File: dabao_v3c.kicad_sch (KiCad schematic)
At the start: 67 parts, among them J1 USB_C_Receptacle_USB2.0_16P, Q1 LP0404N3T5G, Q2 LN237N3T5G, SW1 SKTAAAE010, SW2 SKTAAAE010, U1 baochip1x, U3 SMD IC PMIC;DCDC Buck-ADJ-1A,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, U4 XIAO-HALF-HOLE-23P, U5 EMS4000RSW, U7 SGM40567-4.2XG/TR, U8 SX1801CCR, U9 SMD IC PMIC;DCDC Buck-ADJ-1A,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, Y2 48.000MHz

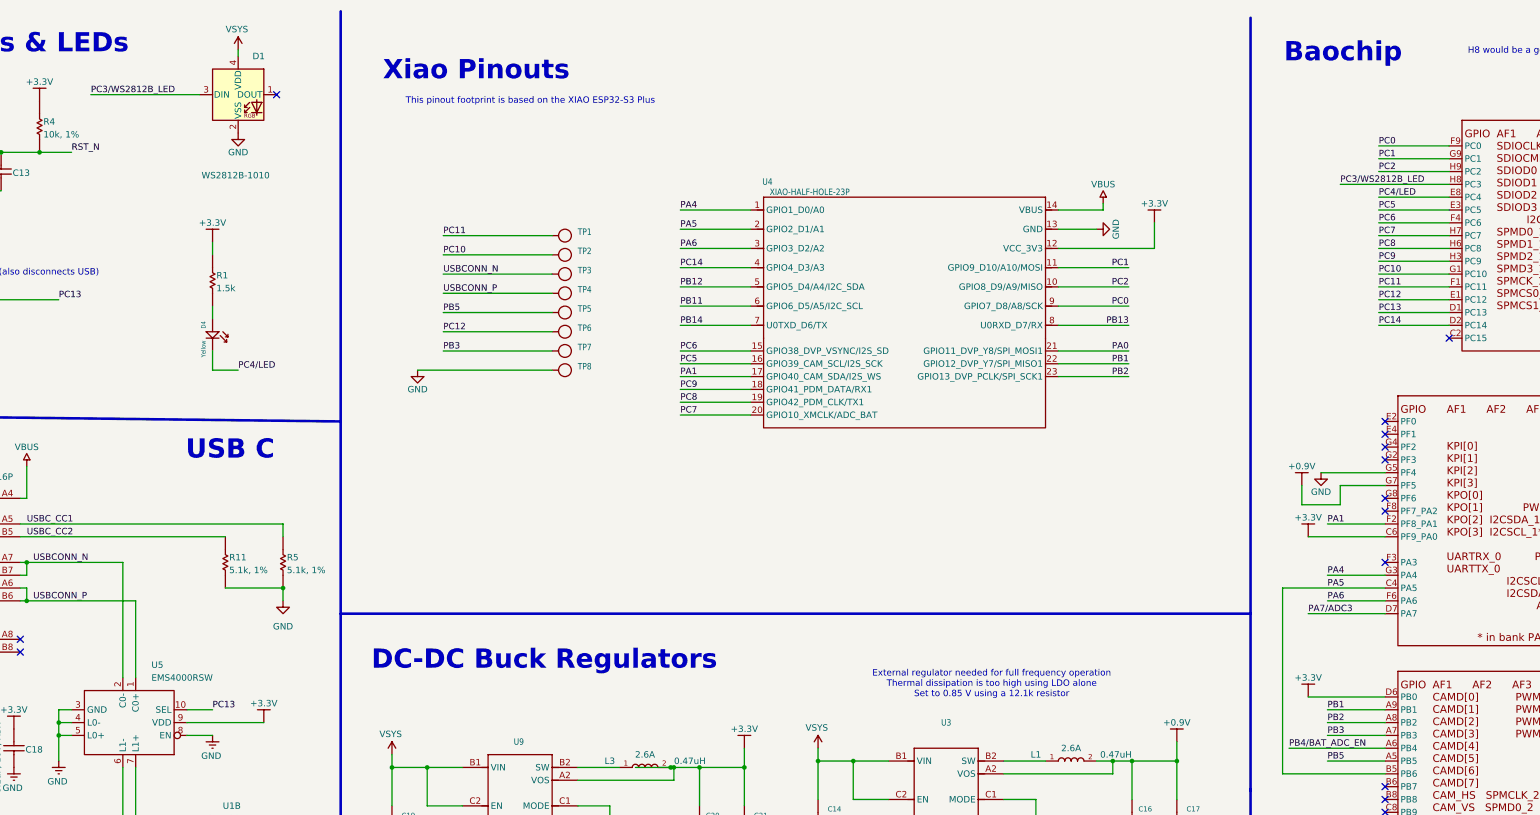
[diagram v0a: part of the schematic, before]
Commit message: with pc0-pc9 and pb11-pb14
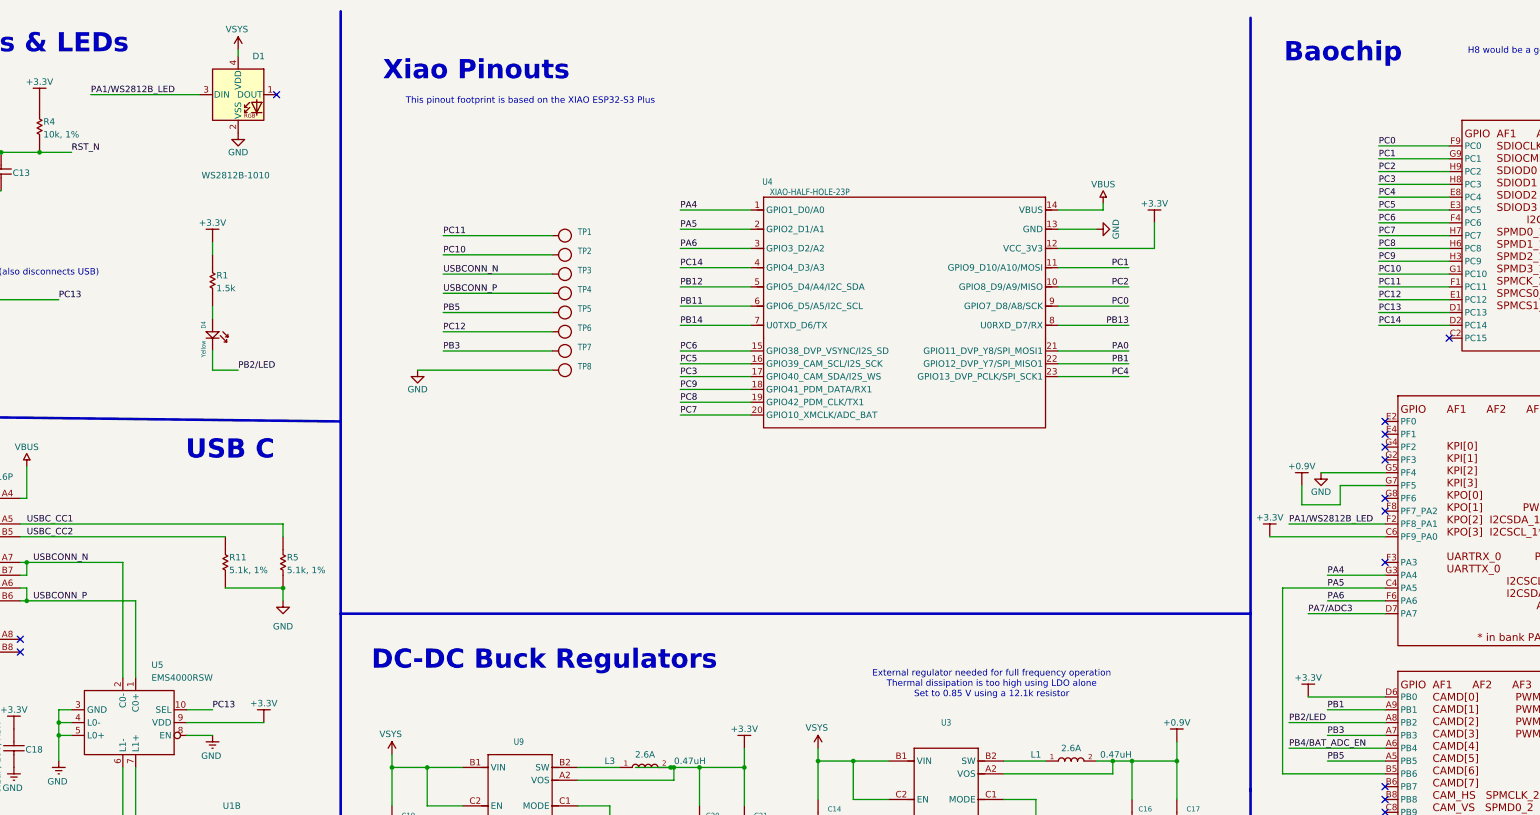
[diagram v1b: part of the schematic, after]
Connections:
- net PA1 renamed PA1/WS2812B_LED
- net PA1/WS2812B_LED: now also D1.3 (DIN); no longer U4.17 (GPIO40_CAM_SDA/I2S_WS)
- net PB2 renamed PB2/LED
- net PB2/LED: now also D4.-; no longer U4.23 (GPIO13_DVP_PCLK/SPI_SCK1)
- net PC3/WS2812B_LED renamed PC3
- net PC3: now also U4.17 (GPIO40_CAM_SDA/I2S_WS); no longer D1.3 (DIN)
- net PC4/LED renamed PC4
- net PC4: now also U4.23 (GPIO13_DVP_PCLK/SPI_SCK1); no longer D4.-
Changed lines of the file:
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@@
 	(wire
 		(pts
-			(xy 311.15 116.84) (xy 326.39 116.84)
+			(xy 303.53 116.84) (xy 326.39 116.84)
 		)
 		(stroke
@@
 	(wire
 		(pts
+			(xy 325.12 46.99) (xy 339.09 46.99)
+		)
+		(stroke
+			(width 0)
+			(type default)
+		)
+	)
+	(wire
+		(pts
 			(xy 165.1 243.84) (xy 165.1 256.54)
 		)
@@
 	(wire
 		(pts
+			(xy 307.34 153.67) (xy 326.39 153.67)
+		)
+		(stroke
+			(width 0)
+			(type default)
+		)
+	)
+	(wire
+		(pts
 			(xy 67.31 209.55) (xy 71.12 209.55)
 		)
@@
 	(wire
 		(pts
+			(xy 307.34 114.3) (xy 326.39 114.3)
+		)
+		(stroke
+			(width 0)
+			(type default)
+		)
+	)
+	(wire
+		(pts
 			(xy 109.22 260.35) (xy 110.49 260.35)
 		)
@@
 	(wire
 		(pts
-			(xy 314.96 114.3) (xy 326.39 114.3)
-		)
-		(stroke
-			(width 0)
-			(type default)
-		)
-	)
-	(wire
-		(pts
 			(xy 21.59 40.64) (xy 26.67 40.64)
 		)
@@
 	(wire
 		(pts
-			(xy 314.96 153.67) (xy 326.39 153.67)
+			(xy 369.57 209.55) (xy 369.57 212.09)
 		)
 		(stroke
@@
 	(wire
 		(pts
-			(xy 369.57 209.55) (xy 369.57 212.09)
+			(xy 325.12 64.77) (xy 339.09 64.77)
 		)
 		(stroke
@@
 	(wire
 		(pts
-			(xy 325.12 64.77) (xy 339.09 64.77)
+			(xy 314.96 161.29) (xy 326.39 161.29)
 		)
 		(stroke
@@
 	(wire
 		(pts
-			(xy 317.5 46.99) (xy 339.09 46.99)
-		)
-		(stroke
-			(width 0)
-			(type default)
-		)
-	)
-	(wire
-		(pts
 			(xy 392.43 214.63) (xy 392.43 217.17)
 		)
@@
 	(wire
 		(pts
-			(xy 314.96 161.29) (xy 326.39 161.29)
-		)
-		(stroke
-			(width 0)
-			(type default)
-		)
-	)
-	(wire
-		(pts
 			(xy 217.805 252.73) (xy 217.805 255.27)
 		)
@@
 		)
 	)
-	(label "PC3{slash}WS2812B_LED"
-		(at 317.5 46.99 0)
-		(effects
-			(font
-				(size 1.27 1.27)
-			)
-			(justify left bottom)
-		)
-	)
 	(label "PC10"
 		(at 325.12 64.77 0)
@@
 		)
 	)
+	(label "PC4"
+		(at 275.59 85.09 180)
+		(effects
+			(font
+				(size 1.27 1.27)
+			)
+			(justify right bottom)
+		)
+	)
 	(label "PB13"
 		(at 314.96 181.61 0)
@@
 		)
 	)
-	(label "XO_48M"
-		(at 72.39 203.2 0)
+	(label "PB5"
+		(at 139.7 72.39 0)
 		(effects
 			(font
@@
 		)
 	)
-	(label "PC5"
-		(at 186.69 82.55 0)
+	(label "XO_48M"
+		(at 72.39 203.2 0)
 		(effects
 			(font
@@
 		)
 	)
-	(label "USBCONN_P"
-		(at 58.42 129.54 0)
+	(label "PC5"
+		(at 186.69 82.55 0)
 		(effects
 			(font
@@
 		)
 	)
-	(label "PC4{slash}LED"
-		(at 325.12 49.53 0)
+	(label "USBCONN_P"
+		(at 58.42 129.54 0)
 		(effects
 			(font
@@
 		)
 	)
-	(label "PC4{slash}LED"
-		(at 99.06 83.82 0)
+	(label "PB12"
+		(at 186.69 67.31 0)
 		(effects
 			(font
@@
 		)
 	)
-	(label "PB12"
-		(at 186.69 67.31 0)
+	(label "PB5"
+		(at 314.96 161.29 0)
 		(effects
 			(font
@@
 		)
 	)
-	(label "PC3{slash}WS2812B_LED"
-		(at 69.85 29.21 0)
+	(label "PC13"
+		(at 93.98 151.13 0)
 		(effects
 			(font
@@
 		)
 	)
-	(label "PC13"
-		(at 93.98 151.13 0)
+	(label "PC3"
+		(at 325.12 46.99 0)
 		(effects
 			(font
@@
 		)
 	)
+	(label "PA1{slash}WS2812B_LED"
+		(at 69.85 29.21 0)
+		(effects
+			(font
+				(size 1.27 1.27)
+			)
+			(justify left bottom)
+		)
+	)
 	(label "PB14"
 		(at 186.69 74.93 0)
@@
 		)
 	)
-	(label "PB2"
-		(at 275.59 85.09 180)
+	(label "PB11"
+		(at 314.96 176.53 0)
 		(effects
 			(font
 				(size 1.27 1.27)
 			)
-			(justify right bottom)
+			(justify left bottom)
 		)
 	)
-	(label "PB5"
-		(at 314.96 161.29 0)
+	(label "PB14"
+		(at 314.96 184.15 0)
 		(effects
 			(font
@@
 		)
 	)
-	(label "PB11"
-		(at 314.96 176.53 0)
+	(label "PC4"
+		(at 325.12 49.53 0)
 		(effects
 			(font
@@
 		)
 	)
-	(label "PB14"
-		(at 314.96 184.15 0)
+	(label "PB2{slash}LED"
+		(at 99.06 83.82 0)
 		(effects
 			(font
@@
 		)
 	)
-	(label "PA1"
-		(at 186.69 85.09 0)
+	(label "PC0"
+		(at 275.59 71.12 180)
 		(effects
 			(font
 				(size 1.27 1.27)
 			)
-			(justify left bottom)
+			(justify right bottom)
 		)
 	)
-	(label "PC0"
-		(at 275.59 71.12 180)
+	(label "PC13"
+		(at 325.12 72.39 0)
 		(effects
 			(font
 				(size 1.27 1.27)
 			)
-			(justify right bottom)
+			(justify left bottom)
 		)
 	)
-	(label "PC13"
-		(at 325.12 72.39 0)
+	(label "PC3"
+		(at 186.69 85.09 0)
 		(effects
 			(font
@@
 		)
 	)
-	(label "PB2"
-		(at 314.96 153.67 0)
-		(effects
-			(font
-				(size 1.27 1.27)
-			)
-			(justify left bottom)
-		)
-	)
 	(label "PC7"
 		(at 186.69 92.71 0)
@@
 		)
 	)
-	(label "PC5"
-		(at 325.12 52.07 0)
+	(label "PB2{slash}LED"
+		(at 307.34 153.67 0)
 		(effects
 			(font
@@
 		)
 	)
-	(label "PA5"
-		(at 314.96 127 0)
+	(label "PC5"
+		(at 325.12 52.07 0)
 		(effects
 			(font
@@
 		)
 	)
-	(label "PA4"
-		(at 314.96 124.46 0)
+	(label "PA1{slash}WS2812B_LED"
+		(at 307.34 114.3 0)
 		(effects
 			(font
@@
 		)
 	)
-	(label "PA6"
-		(at 314.96 129.54 0)
+	(label "PA5"
+		(at 314.96 127 0)
 		(effects
 			(font
@@
 		)
 	)
-	(label "USBC_CC2"
-		(at 57.15 116.84 0)
+	(label "PA4"
+		(at 314.96 124.46 0)
 		(effects
 			(font
@@
 		)
 	)
-	(label "PA1"
-		(at 314.96 114.3 0)
+	(label "PA6"
+		(at 314.96 129.54 0)
 		(effects
 			(font
@@
 		)
 	)
-	(label "PC11"
-		(at 139.7 57.15 0)
+	(label "USBC_CC2"
+		(at 57.15 116.84 0)
 		(effects
 			(font
@@
 		)
 	)
-	(label "PB5"
-		(at 139.7 72.39 0)
+	(label "PC11"
+		(at 139.7 57.15 0)
 		(effects
 			(font
@@
 	(symbol
 		(lib_id "power-altium-import:P1.8V_BAR")
-		(at 311.15 116.84 180)
+		(at 303.53 116.84 180)
 		(unit 1)
 		(exclude_from_sim no)
@@
 		(dnp no)
 		(property "Reference" "#PWR022"
-			(at 311.15 116.84 0)
+			(at 303.53 116.84 0)
 			(effects
 				(font
@@
 		)
 		(property "Value" "+3.3V"
-			(at 311.15 113.03 0)
+			(at 303.53 113.03 0)
 			(effects
 				(font
@@
 		)
 		(property "Footprint" ""
-			(at 311.15 116.84 0)
+			(at 303.53 116.84 0)
 			(effects
 				(font
@@
 		)
 		(property "Datasheet" ""
-			(at 311.15 116.84 0)
+			(at 303.53 116.84 0)
 			(effects
 				(font
@@
 		)
 		(property "Description" ""
-			(at 311.15 116.84 0)
+			(at 303.53 116.84 0)
 			(effects
 				(font

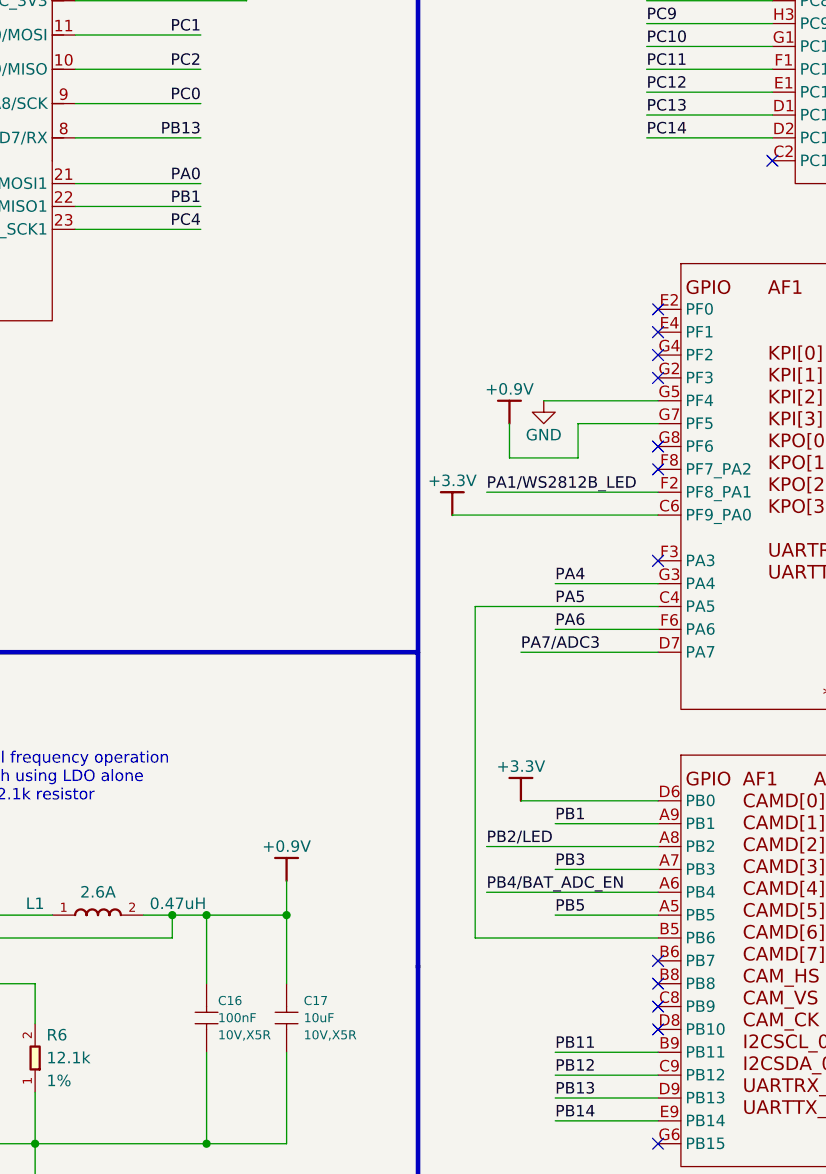
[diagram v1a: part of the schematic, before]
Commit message: fixed the fact that pa0 was a lie
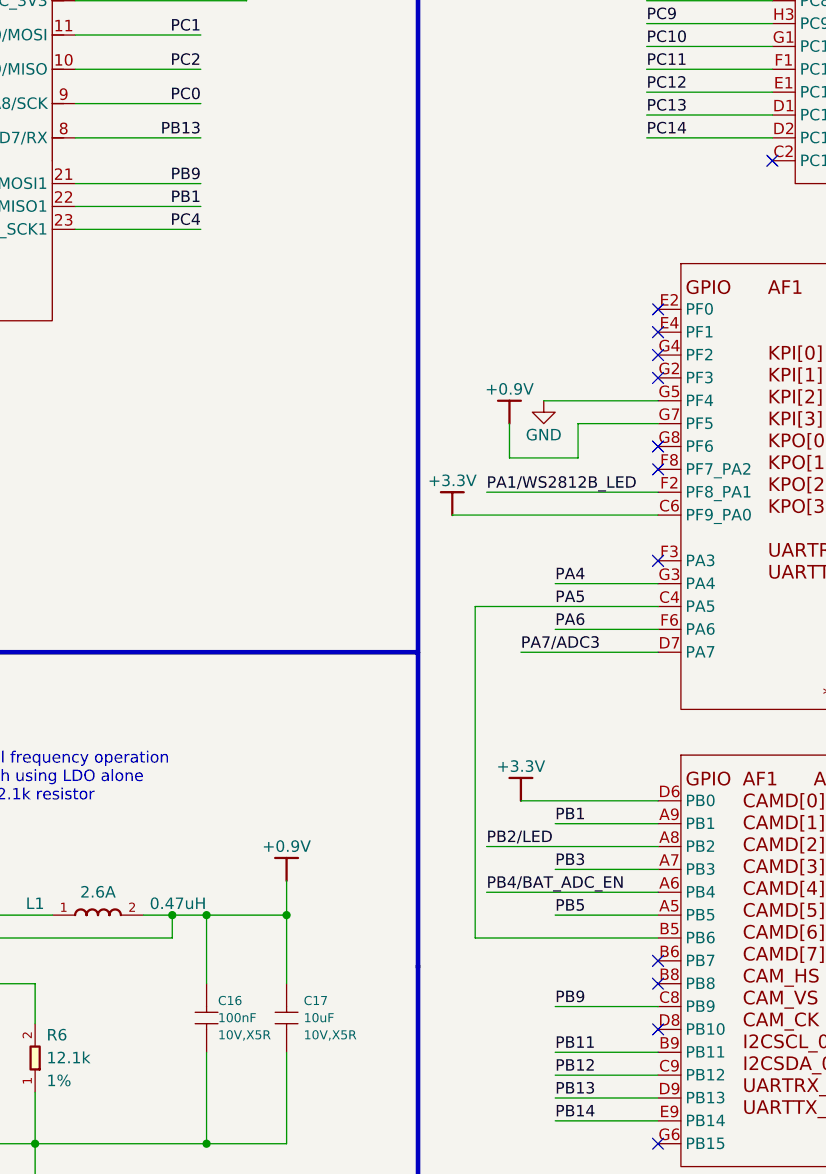
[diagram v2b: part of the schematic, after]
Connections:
- net PA0 is gone; now on net PB9: U4.21 (GPIO11_DVP_Y8/SPI_MOSI1)
- net PB9: now reaches U1.C8 (PB9)
- no-connect marks 19 -> 18
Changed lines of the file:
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@@
 	)
 	(no_connect
-		(at 326.39 171.45)
-	)
-	(no_connect
 		(at 55.88 139.7)
 	)
@@
 	(wire
 		(pts
+			(xy 314.96 171.45) (xy 326.39 171.45)
+		)
+		(stroke
+			(width 0)
+			(type default)
+		)
+	)
+	(wire
+		(pts
 			(xy 190.5 187.96) (xy 172.72 187.96)
 		)
@@
 		)
 	)
+	(label "PB9"
+		(at 314.96 171.45 0)
+		(effects
+			(font
+				(size 1.27 1.27)
+			)
+			(justify left bottom)
+		)
+	)
 	(label "PA7{slash}ADC3"
 		(at 191.77 256.54 180)
@@
 		)
 	)
-	(label "PA0"
-		(at 275.59 80.01 180)
-		(effects
-			(font
-				(size 1.27 1.27)
-			)
-			(justify right bottom)
-		)
-	)
 	(label "PC2"
 		(at 275.59 67.31 180)
@@
 		)
 	)
+	(label "PB9"
+		(at 275.59 80.01 180)
+		(effects
+			(font
+				(size 1.27 1.27)
+			)
+			(justify right bottom)
+		)
+	)
